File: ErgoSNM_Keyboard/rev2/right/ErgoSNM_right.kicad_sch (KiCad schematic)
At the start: 23 parts, among them J1 USB_C_Receptacle_USB2.0, J2 USB_C_Receptacle_USB2.0, J3 PJ-393_TRRS_8P, J4 Conn_01x08, U1 RT9013-33GB, U2 SRV05-4

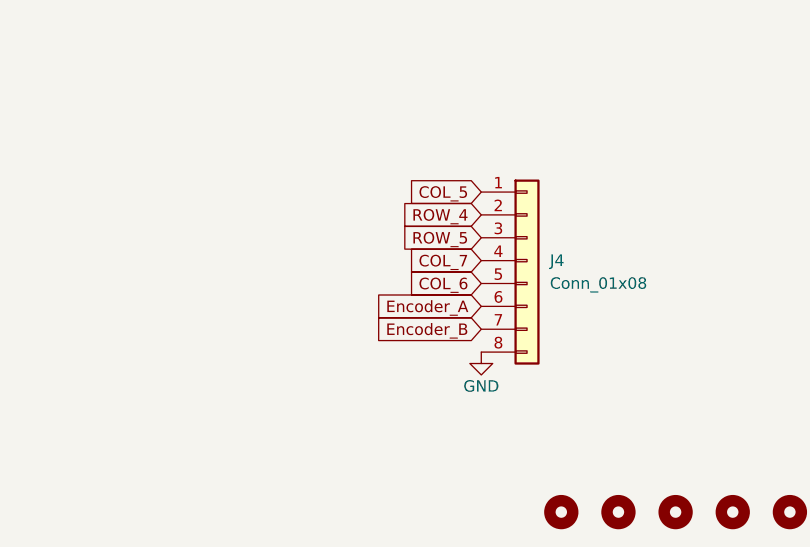
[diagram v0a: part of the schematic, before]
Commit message: Update right hand schematic
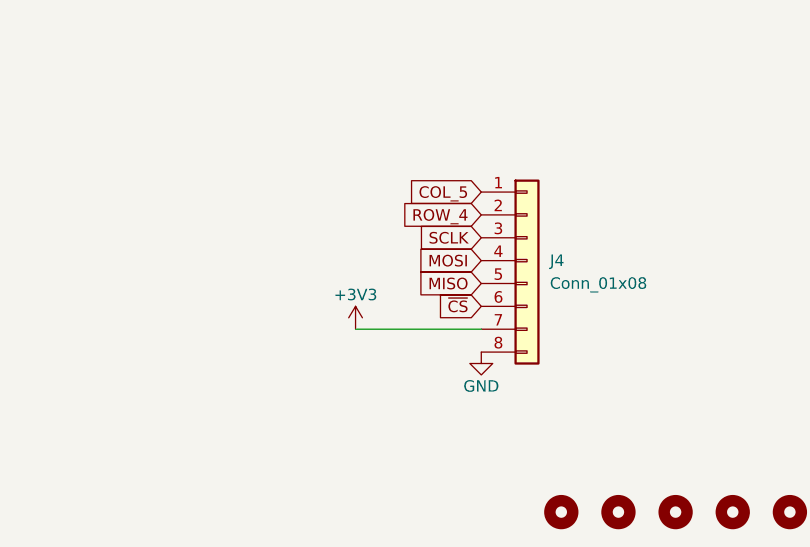
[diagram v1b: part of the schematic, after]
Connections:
- net Encoder_B is gone; now on net +3V3: J4.7 (Pin_7)
- net COL_6 renamed MISO
- net COL_7 renamed MOSI
- net Encoder_A renamed ~{CS}
- net ROW_5 renamed SCLK
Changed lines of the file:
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@@
+    (stroke (width 0) (type default) (color 0 0 0 0))
+  )
+  (wire (pts (xy 119.38 173.99) (xy 133.35 173.99))
     (stroke (width 0) (type default) (color 0 0 0 0))
   )
@@
     )
   )
-  (global_label "Encoder_A" (shape input) (at 133.35 171.45 180) (fields_autoplaced)
+  (global_label "MOSI" (shape input) (at 133.35 166.37 180) (fields_autoplaced)
     (effects (font (size 1.27 1.27)) (justify right))
-    (property "Intersheet References" "${INTERSHEET_REFS}" (id 0) (at 121.3212 171.3706 0)
+    (property "Intersheet References" "${INTERSHEET_REFS}" (id 0) (at 126.3407 166.2906 0)
       (effects (font (size 1.27 1.27)) (justify right) hide)
     )
   )
-  (global_label "ROW_5" (shape input) (at 133.35 163.83 180) (fields_autoplaced)
+  (global_label "MISO" (shape input) (at 133.35 168.91 180) (fields_autoplaced)
     (effects (font (size 1.27 1.27)) (justify right))
-    (property "Intersheet References" "${INTERSHEET_REFS}" (id 0) (at 124.7079 163.7506 0)
-      (effects (font (size 1.27 1.27)) (justify right) hide)
-    )
-  )
-  (global_label "Encoder_B" (shape input) (at 133.35 173.99 180) (fields_autoplaced)
-    (effects (font (size 1.27 1.27)) (justify right))
-    (property "Intersheet References" "${INTERSHEET_REFS}" (id 0) (at 121.1398 173.9106 0)
+    (property "Intersheet References" "${INTERSHEET_REFS}" (id 0) (at 126.3407 168.8306 0)
       (effects (font (size 1.27 1.27)) (justify right) hide)
     )
@@
     )
   )
-  (global_label "COL_7" (shape input) (at 133.35 166.37 180) (fields_autoplaced)
+  (global_label "~{CS}" (shape input) (at 133.35 171.45 180) (fields_autoplaced)
     (effects (font (size 1.27 1.27)) (justify right))
-    (property "Intersheet References" "${INTERSHEET_REFS}" (id 0) (at 125.1312 166.2906 0)
+    (property "Intersheet References" "${INTERSHEET_REFS}" (id 0) (at 128.4574 171.3706 0)
       (effects (font (size 1.27 1.27)) (justify right) hide)
     )
@@
     )
   )
-  (global_label "COL_6" (shape input) (at 133.35 168.91 180) (fields_autoplaced)
+  (global_label "SCLK" (shape input) (at 133.35 163.83 180) (fields_autoplaced)
     (effects (font (size 1.27 1.27)) (justify right))
-    (property "Intersheet References" "${INTERSHEET_REFS}" (id 0) (at 125.1312 168.8306 0)
+    (property "Intersheet References" "${INTERSHEET_REFS}" (id 0) (at 126.1593 163.7506 0)
       (effects (font (size 1.27 1.27)) (justify right) hide)
     )
@@
     (pin "2")
   )
+  (symbol (lib_id "power:+3V3") (at 119.38 173.99 0) (unit 1)
+    (in_bom yes) (on_board yes)
+    (property "Reference" "#PWR?" (id 0) (at 119.38 177.8 0)
+      (effects (font (size 1.27 1.27)) hide)
+    )
+    (property "Value" "+3V3" (id 1) (at 119.38 170.18 0))
+    (property "Footprint" "" (id 2) (at 119.38 173.99 0)
+      (effects (font (size 1.27 1.27)) hide)
+    )
+    (property "Datasheet" "" (id 3) (at 119.38 173.99 0)
+      (effects (font (size 1.27 1.27)) hide)
+    )
+    (pin "1")
+  )
   (symbol (lib_id "power:VBUS") (at 57.15 30.48 0) (unit 1)
     (in_bom yes) (on_board yes)
@@
       (reference "#PWR027") (unit 1) (value "GND") (footprint "")
     )
-    (path "/3bf993f0-d9b3-4b1c-995c-23aac1b6e6f2/ff5d944f-2f8f-4429-b3b4-43d77de5b092"
-      (reference "#PWR028") (unit 1) (value "+3V3") (footprint "")
-    )
     (path "/3bf993f0-d9b3-4b1c-995c-23aac1b6e6f2/e2e345cf-d245-45ac-a887-6cee31ac752c"
       (reference "#PWR029") (unit 1) (value "GND") (footprint "")
@@
       (reference "#PWR039") (unit 1) (value "GND") (footprint "")
     )
+    (path "/3bf993f0-d9b3-4b1c-995c-23aac1b6e6f2/46083f80-8278-4223-8ea4-b4157e358430"
+      (reference "#PWR?") (unit 1) (value "GND") (footprint "")
+    )
+    (path "/babe1564-f105-4acf-8c1e-3afedac09525"
+      (reference "#PWR?") (unit 1) (value "+3V3") (footprint "")
+    )
     (path "/2a3c100f-0045-4b2b-99e5-091d1d541755"

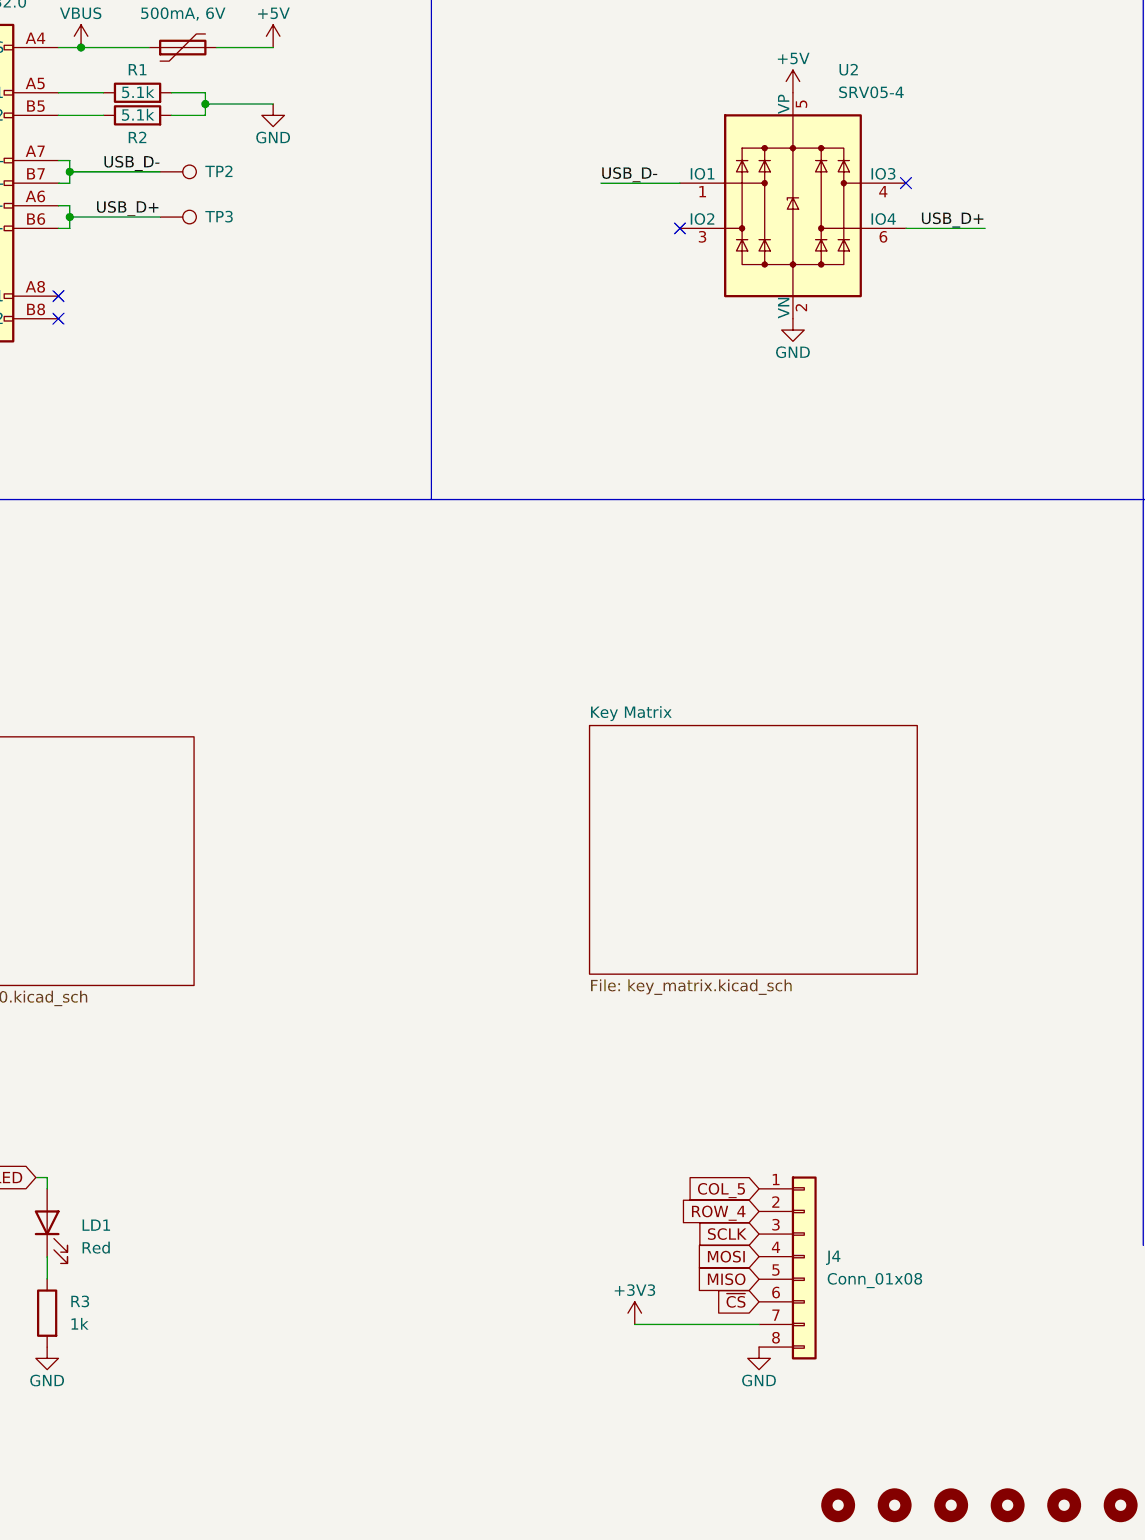
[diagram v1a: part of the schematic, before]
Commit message: Update right PCB
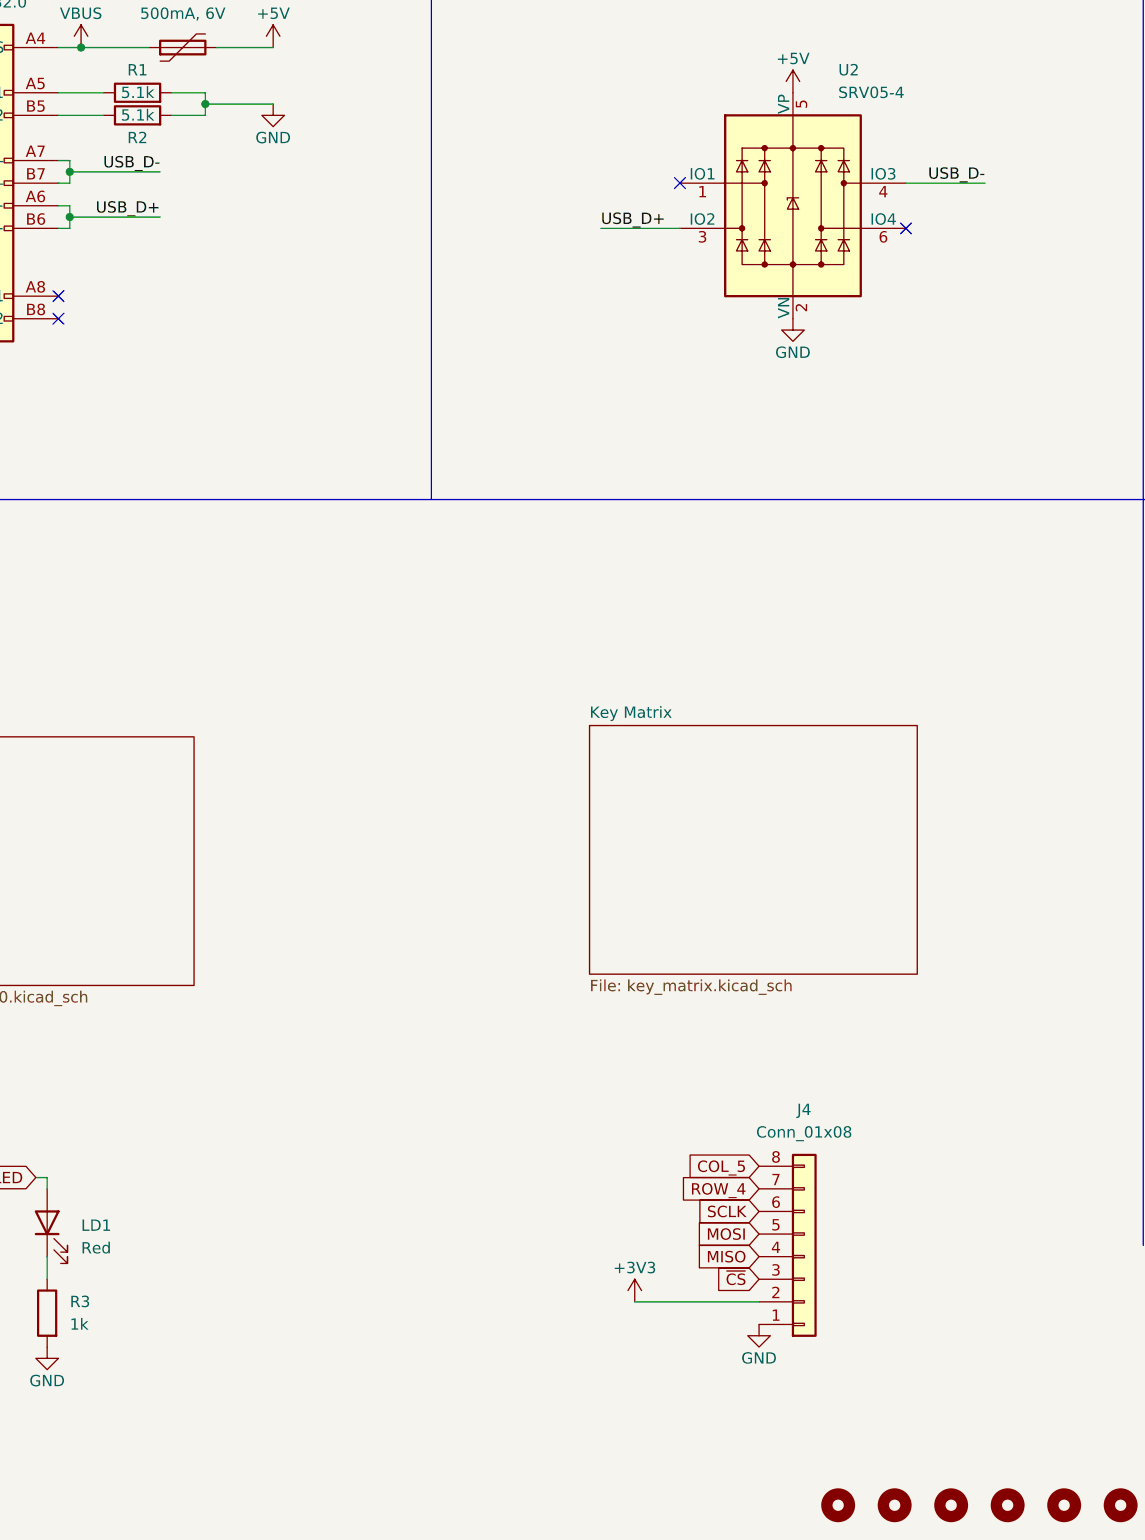
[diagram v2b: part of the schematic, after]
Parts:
- removed TP2, TP3: TestPoint, TestPoint:TestPoint_Pad_D2.0mm, symbol Connector:TestPoint
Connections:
- net +3V3: now also J4.2 (Pin_2); no longer J4.7 (Pin_7)
- net COL_5: now also J4.8 (Pin_8); no longer J4.1 (Pin_1)
- net GND: now also J4.1 (Pin_1); no longer J4.8 (Pin_8)
- net MISO: now also J4.4 (Pin_4); no longer J4.5 (Pin_5)
- net MOSI: now also J4.5 (Pin_5); no longer J4.4 (Pin_4)
- net ROW_4: now also J4.7 (Pin_7); no longer J4.2 (Pin_2)
- net SCLK: now also J4.6 (Pin_6); no longer J4.3 (Pin_3)
- net USB_D+: now also U2.3 (IO2); no longer U2.6 (IO4)
- net USB_D-: now also U2.4 (IO3); no longer U2.1 (IO1)
- net ~{CS}: now also J4.3 (Pin_3); no longer J4.6 (Pin_6)
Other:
- moved on the sheet: J4

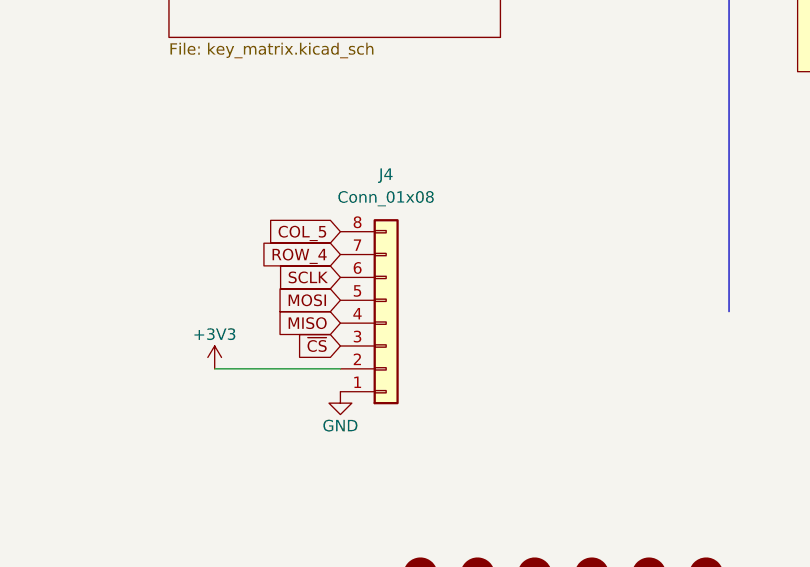
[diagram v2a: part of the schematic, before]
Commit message: Replace JST GH 1.25 connector with 0.5mm FPC
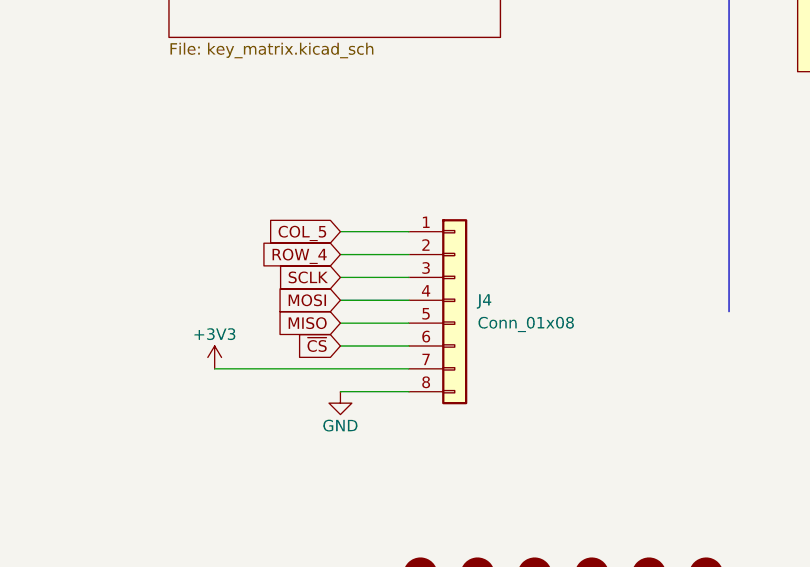
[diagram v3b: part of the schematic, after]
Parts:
- J4: footprint Connector_JST:JST_GH_SM08B-GHS-TB_1x08-1MP_P1.25mm_Horizontal -> ErgoSNM_Keyboard:FPC_8P_0.5mm_AFC01-S08FCA-00
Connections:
- net +3V3: now also J4.7 (Pin_7); no longer J4.2 (Pin_2)
- net COL_5: now also J4.1 (Pin_1); no longer J4.8 (Pin_8)
- net GND: now also J4.8 (Pin_8); no longer J4.1 (Pin_1)
- net MISO: now also J4.5 (Pin_5); no longer J4.4 (Pin_4)
- net MOSI: now also J4.4 (Pin_4); no longer J4.5 (Pin_5)
- net ROW_4: now also J4.2 (Pin_2); no longer J4.7 (Pin_7)
- net SCLK: now also J4.3 (Pin_3); no longer J4.6 (Pin_6)
- net ~{CS}: now also J4.6 (Pin_6); no longer J4.3 (Pin_3)
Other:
- moved on the sheet: J4
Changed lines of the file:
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@@
   (title_block
     (title "ErgoSNM Keyboard - Right")
-    (rev "2.0")
+    (rev "2.1")
     (comment 1 "MIT License (Open source hardware)")
     (comment 2 "https://github.com/ziteh/ergo-snm-keyboard")
@@
     (stroke (width 0) (type default) (color 0 0 0 0))
   )
+  (wire (pts (xy 119.38 171.45) (xy 140.97 171.45))
+    (stroke (width 0) (type default) (color 0 0 0 0))
+  )
   (wire (pts (xy 71.12 36.83) (xy 71.12 38.1))
     (stroke (width 0) (type default) (color 0 0 0 0))
   )
+  (wire (pts (xy 140.97 158.75) (xy 133.35 158.75))
+    (stroke (width 0) (type default) (color 0 0 0 0))
+  )
   (wire (pts (xy 59.69 35.56) (xy 54.61 35.56))
     (stroke (width 0) (type default) (color 0 0 0 0))
   )
+  (wire (pts (xy 140.97 161.29) (xy 133.35 161.29))
+    (stroke (width 0) (type default) (color 0 0 0 0))
+  )
   (wire (pts (xy 115.57 50.8) (xy 124.46 50.8))
     (stroke (width 0) (type default) (color 0 0 0 0))
@@
     (stroke (width 0) (type default) (color 0 0 0 0))
   )
+  (wire (pts (xy 140.97 168.91) (xy 133.35 168.91))
+    (stroke (width 0) (type default) (color 0 0 0 0))
+  )
   (wire (pts (xy 212.09 43.18) (xy 212.09 45.72))
     (stroke (width 0) (type default) (color 0 0 0 0))
@@
     (stroke (width 0) (type default) (color 0 0 0 0))
   )
-  (wire (pts (xy 119.38 171.45) (xy 133.35 171.45))
-    (stroke (width 0) (type default) (color 0 0 0 0))
-  )
   (wire (pts (xy 54.61 30.48) (xy 57.15 30.48))
     (stroke (width 0) (type default) (color 0 0 0 0))
@@
     (stroke (width 0) (type default) (color 0 0 0 0))
   )
+  (wire (pts (xy 140.97 163.83) (xy 133.35 163.83))
+    (stroke (width 0) (type default) (color 0 0 0 0))
+  )
   (wire (pts (xy 55.88 44.45) (xy 55.88 45.72))
     (stroke (width 0) (type default) (color 0 0 0 0))
@@
     (stroke (width 0) (type default) (color 0 0 0 0))
   )
+  (wire (pts (xy 140.97 166.37) (xy 133.35 166.37))
+    (stroke (width 0) (type default) (color 0 0 0 0))
+  )
   (wire (pts (xy 53.34 158.75) (xy 53.34 157.48))
     (stroke (width 0) (type default) (color 0 0 0 0))
@@
     (stroke (width 0) (type default) (color 0 0 0 0))
   )
+  (wire (pts (xy 140.97 156.21) (xy 133.35 156.21))
+    (stroke (width 0) (type default) (color 0 0 0 0))
+  )
   (wire (pts (xy 217.17 48.26) (xy 217.17 43.18))
     (stroke (width 0) (type default) (color 0 0 0 0))
@@
   )
   (wire (pts (xy 78.74 30.48) (xy 72.39 30.48))
+    (stroke (width 0) (type default) (color 0 0 0 0))
+  )
+  (wire (pts (xy 140.97 173.99) (xy 133.35 173.99))
     (stroke (width 0) (type default) (color 0 0 0 0))
   )
@@
     (pin "1")
   )
-  (symbol (lib_id "Connector_Generic:Conn_01x08") (at 138.43 166.37 0) (mirror x) (unit 1)
+  (symbol (lib_id "Connector_Generic:Conn_01x08") (at 146.05 163.83 0) (unit 1)
     (in_bom yes) (on_board yes) (fields_autoplaced)
-    (property "Reference" "J4" (id 0) (at 138.43 149.86 0))
-    (property "Value" "Conn_01x08" (id 1) (at 138.43 152.4 0))
-    (property "Footprint" "Connector_JST:JST_GH_SM08B-GHS-TB_1x08-1MP_P1.25mm_Horizontal" (id 2) (at 138.43 166.37 0)
-      (effects (font (size 1.27 1.27)) hide)
-    )
-    (property "Datasheet" "~" (id 3) (at 138.43 166.37 0)
-      (effects (font (size 1.27 1.27)) hide)
-    )
-    (property "LCSC" "C265111" (id 4) (at 138.43 166.37 0)
-      (effects (font (size 1.27 1.27)) hide)
-    )
-    (property "MFR. Part #" "SM08B-GHS-TB(LF)(SN)" (id 5) (at 138.43 166.37 0)
+    (property "Reference" "J4" (id 0) (at 148.59 163.8299 0)
+      (effects (font (size 1.27 1.27)) (justify left))
+    )
+    (property "Value" "Conn_01x08" (id 1) (at 148.59 166.3699 0)
+      (effects (font (size 1.27 1.27)) (justify left))
+    )
+    (property "Footprint" "ErgoSNM_Keyboard:FPC_8P_0.5mm_AFC01-S08FCA-00" (id 2) (at 146.05 163.83 0)
+      (effects (font (size 1.27 1.27)) hide)
+    )
+    (property "Datasheet" "~" (id 3) (at 146.05 163.83 0)
+      (effects (font (size 1.27 1.27)) hide)
+    )
+    (property "LCSC" "C265111" (id 4) (at 146.05 163.83 0)
+      (effects (font (size 1.27 1.27)) hide)
+    )
+    (property "MFR. Part #" "SM08B-GHS-TB(LF)(SN)" (id 5) (at 146.05 163.83 0)
       (effects (font (size 1.27 1.27)) hide)
     )
@@
     )
     (path "/d0686554-530b-491a-bdc9-ed48c45d810a"
-      (reference "J4") (unit 1) (value "Conn_01x08") (footprint "Connector_JST:JST_GH_SM08B-GHS-TB_1x08-1MP_P1.25mm_Horizontal")
+      (reference "J4") (unit 1) (value "Conn_01x08") (footprint "ErgoSNM_Keyboard:FPC_8P_0.5mm_AFC01-S08FCA-00")
     )
     (path "/1a54857c-0204-45b8-b08f-47236e02c723/bef0ed30-218e-42e5-9109-965e80a536d2"
